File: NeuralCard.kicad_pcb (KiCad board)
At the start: 2 copper layers, 85.6 x 54 mm, 54 parts, among them J1 ProgPads, SW1 SW-SMD_4P-L5.1-W5.1-P3.70-LS6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, SW2 SW-SMD_4P-L5.1-W5.1-P3.70-LS6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, SW3 SW_SPDT_Shouhan_MSK12C02, U1 WIRELM-SMD_ESP32-S3-WROOM-1, U2 LGA-14_L3.0-W2.5-P0.50-TL, U4 SO-8_L4.9-W3.9-P1.27-LS5.9-BL

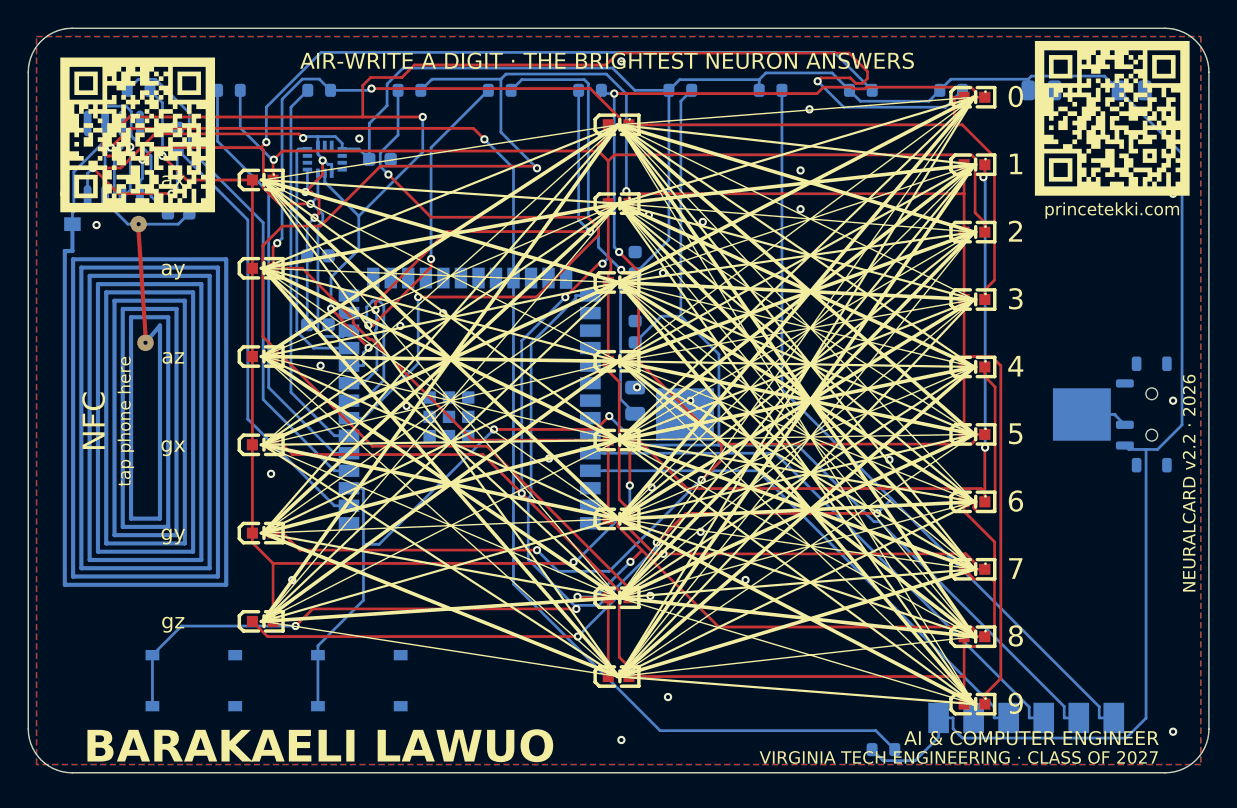
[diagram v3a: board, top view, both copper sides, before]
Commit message: fix: fiducials and courtyard
Two findings from the first full analyzer run against the v2.2 board.

The NFC coil footprint carried allow_missing_courtyard, so placement checkers
had nothing to measure and fell back to the footprint origin at (0,0), which is
the board corner -- hence "ANT1 is 0.0mm from board edge". The coil copper
actually sits 2.65mm inboard. The reading was wrong but the cause was a real
defect: a footprint with no courtyard cannot be collision-checked. Now emits a
B.CrtYd box around the drawn extent plus the standard 0.25mm margin. C12 moved
13.4 -> 12.9 because the new courtyard clipped its by 0.1mm.

Adds three Fiducial_1mm_Mask2mm targets on B.Cu in an L pattern, asymmetric so
the placement machine cannot mistake orientation. Excluded from BOM and CPL, so
the count stays 52. Justified by the 0.28mm minimum pad on the LGA-14 IMU.

Verification: 100% routed (score 995.36), PCB analyzer errors 2 -> 0, findings
13 -> 11 with both remaining being warnings, 586 tracks, DRC 0 clearance and 0
crossing and 0 courtyard-overlap. Isolated GND pour islands 28 -> 27, still the
open regression from v2.2.

Still open: R14 at 0.95mm from board edge, and TE-001 test points which does not
apply to a business card.
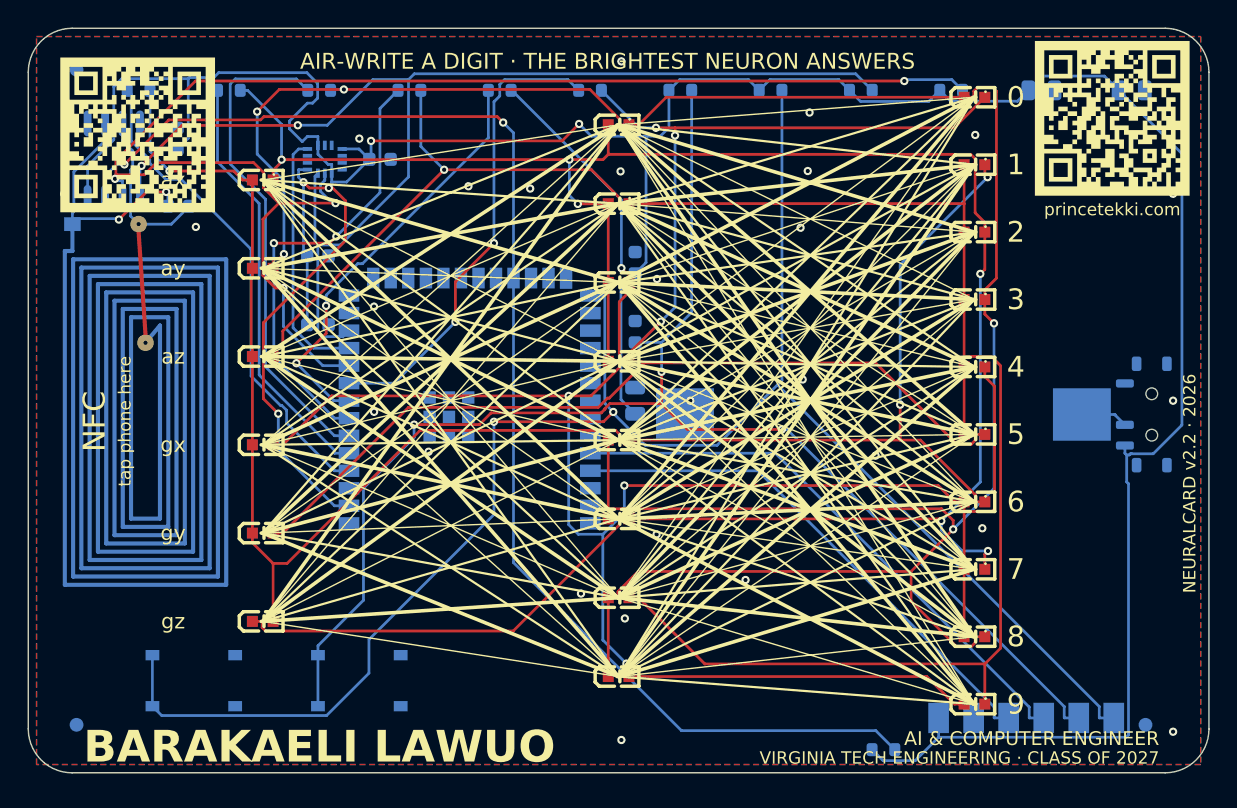
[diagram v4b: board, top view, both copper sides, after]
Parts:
- added FID1: Fiducial_1mm_Mask2mm, Fiducial_1mm_Mask2mm, B.Cu at (3.50, 3.00)
- added FID2: Fiducial_1mm_Mask2mm, Fiducial_1mm_Mask2mm, B.Cu at (3.50, 50.5)
- added FID3: Fiducial_1mm_Mask2mm, Fiducial_1mm_Mask2mm, B.Cu at (81.0, 50.5)
- moved C12 0.50 mm to (10.9, 12.9)
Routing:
- net CP4: track 167.5 -> 139.8 mm, vias 2 -> 1
- net CHX4: track 50.6 -> 32.7 mm
- net CP3: track 161.7 -> 178.6 mm, vias 4 -> 5
- net CP5: track 136.4 -> 151.8 mm
- net IO0: track 144.9 -> 132.7 mm, vias 4 -> 2
- net CP2: track 154.6 -> 166.3 mm, vias 3 -> 6
- net SCL: track 114.9 -> 104.7 mm, vias 5 -> 4
- net CHX3: track 27.9 -> 35.8 mm
- net CP6: track 115.9 -> 109.1 mm, vias 4 -> 3
- net EN: track 114.8 -> 108.7 mm, vias 2 -> 3
- net SDA: track 83.4 -> 88.5 mm, vias 3 -> 2
- net CP1: track 129.6 -> 126.4 mm, vias 5 -> 3
- net NFC_ANT_A: track 20.1 -> 17.0 mm, vias 0 -> 2
- net CHX5: track 32.3 -> 30.7 mm
- net CHX1: track 37.2 -> 35.6 mm
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
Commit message: fix: pour islands cleared
Closes out the two items left open at v2.2.1 and syncs the silk with the tag.

stitch_islands.py relaxed the GND pours to AREA-mode island removal so
candidate islands survive long enough to receive a stitching via, but never
restored the strict mode -- every island it could not reach stayed isolated
copper forever (5 -> 27 -> 28 across v2.2/v2.2.1). It now restores
ISLAND_REMOVAL_MODE_ALWAYS after the loop converges and refills: via-stitched
islands are connected and survive, unreachable orphans are purged.

R14 moved 52.3 -> 51.9, putting its courtyard past the 1.0mm handling
recommendation and clearing the silk-edge warning its designator caused.
Silkscreen bumped to v2.2.2 so the board matches the release tag (v2.2.1
shipped marked v2.2).

Verification: 100% routed (score 995.19), DRC 0 violations (v2.1 had 9, v2.2
had 29), PCB analyzer 0 errors and 1 warning (TE-001 test points, N/A for a
business card), 642 tracks, 83 vias, CPL 52 placements. The 5 remaining
unconnected notices are same-net GND zone fragments, identical in kind and
count to the v2.1 baseline.
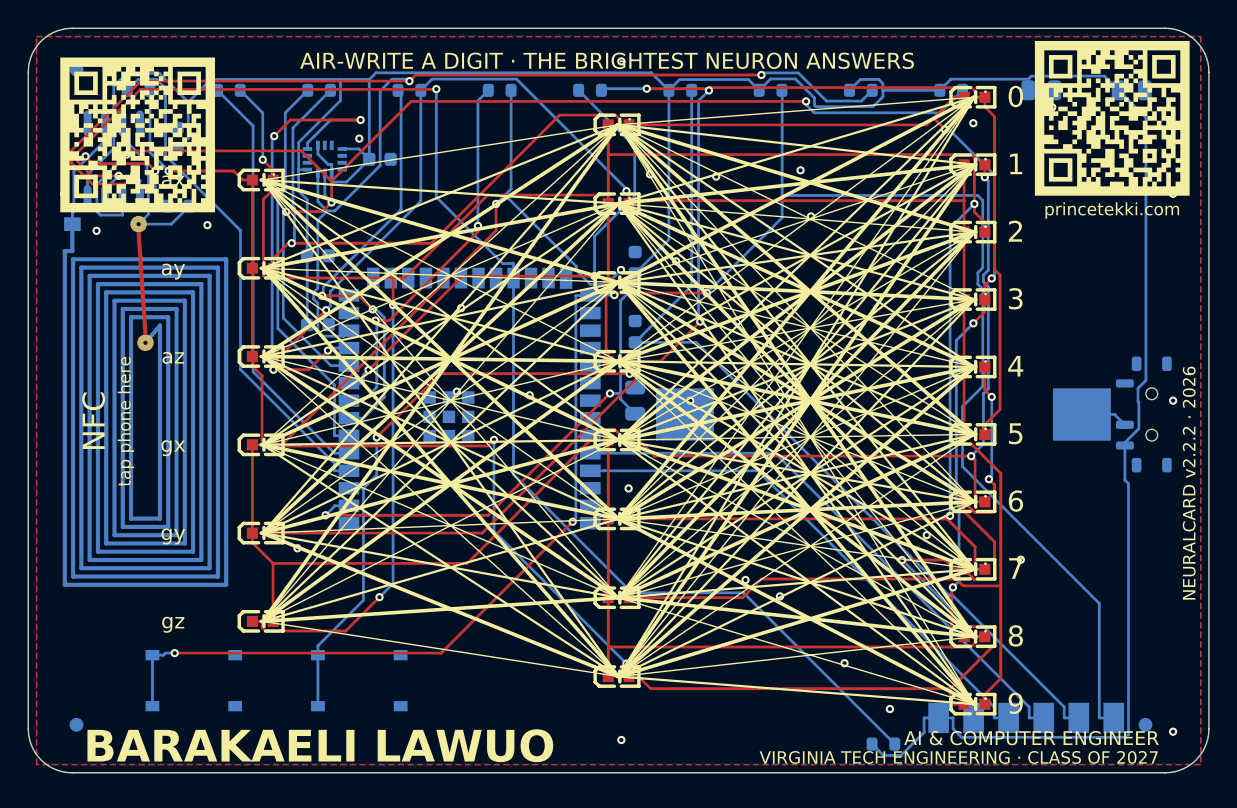
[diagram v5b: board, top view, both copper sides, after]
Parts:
- moved R14 0.40 mm to (62.0, 51.9)
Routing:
- net CP3: track 178.6 -> 155.6 mm
- net IMU_INT: track 18.4 -> 34.9 mm, vias 0 -> 4
- net CP2: track 166.3 -> 178.2 mm, vias 6 -> 5
- net SCL: track 104.7 -> 94.8 mm
- net SDA: track 88.5 -> 97.8 mm, vias 2 -> 3
- net CHX3: track 35.8 -> 28.7 mm
- net IO0: track 132.7 -> 139.5 mm, vias 2 -> 4
- net +3V3: track 247.8 -> 253.2 mm, vias 5 -> 2
- net CHX6: track 34.3 -> 37.7 mm
- net CP4: track 139.8 -> 136.9 mm, vias 1 -> 2
- net CHX5: track 30.7 -> 28.0 mm
- net NFC_GPO: track 97.9 -> 100.5 mm
- net CP1: track 126.4 -> 128.2 mm
- net CHX1: track 35.6 -> 37.2 mm
- net CHX4: track 32.7 -> 31.5 mm
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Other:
- board text added: "NEURALCARD v2.2.2 · 2026"
- board text added: "NeuralCard v2.2.2 · princetekki.com"
- board text removed: "NEURALCARD v2.2 · 2026"
- board text removed: "NeuralCard v2.2 · princetekki.com"
